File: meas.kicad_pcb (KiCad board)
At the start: 2 copper layers, 100 x 135 mm, 218 parts, among them J101 Conn_01x06_Socket, J102 Conn_01x02_Socket, J103 Conn_01x02_Socket, J104 Conn_01x02_Socket, J105 Conn_01x02_Socket, Q1001 DPLS350E, U1001 MC7805, U1101 R05C05TE05S, U1201 R05C05TE05S, U1301 R05C05TE05S, U1401 R05C05TE05S, U201 Si8641BD-B-IS2, U301 Si8641BD-B-IS2, U401 Si8641BD-B-IS2, U501 Si8641BD-B-IS2, U601 ADS8665IPWR, U701 ADS8665IPWR, U801 ADS8665IPWR, U901 ACS730xLCTR-20AB

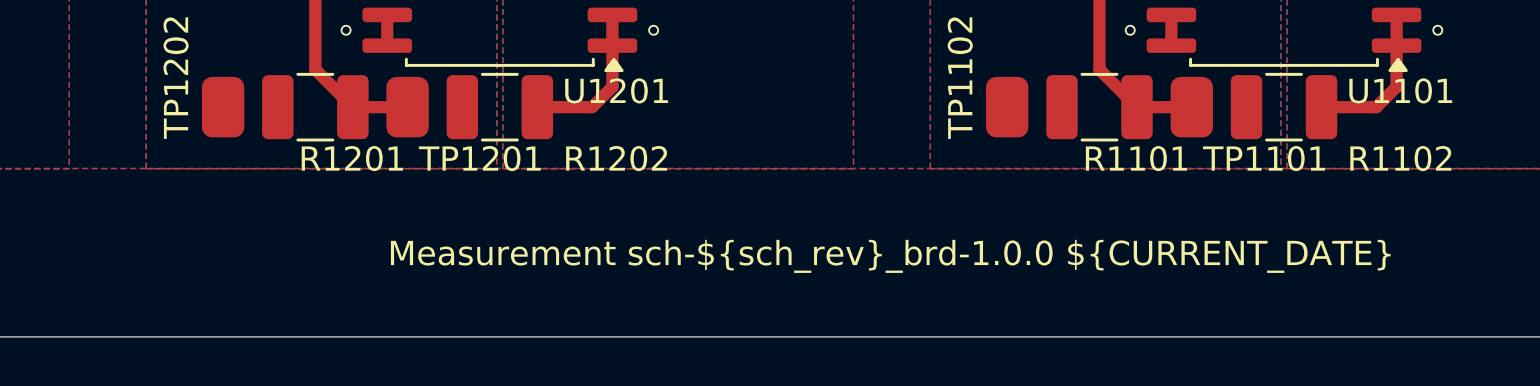
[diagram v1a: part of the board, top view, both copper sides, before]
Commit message: fix netlist error in schematic and layout
GND planes of isodcdc and adc of current measurement were not connected and now are connected.
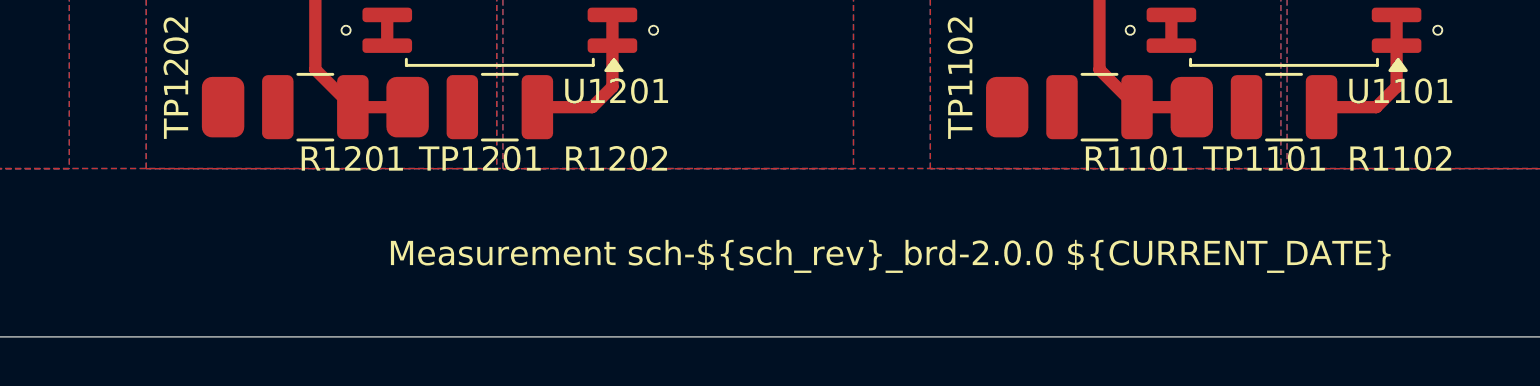
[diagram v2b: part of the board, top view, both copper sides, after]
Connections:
- C1201 pad 1: /adc1/GND_ADC -> /GND_ISO_I
- C1202 pad 1: /adc1/GND_ADC -> /GND_ISO_I
- C701 pad 1: /adc1/GND_ADC -> /GND_ISO_I
- C702 pad 1: /adc1/GND_ADC -> /GND_ISO_I
- C703 pad 1: /adc1/GND_ADC -> /GND_ISO_I
- C705 pad 1: /adc1/GND_ADC -> /GND_ISO_I
- C706 pad 1: /adc1/GND_ADC -> /GND_ISO_I
- C707 pad 1: /adc1/GND_ADC -> /GND_ISO_I
- D1201 pad 2: /adc1/GND_ADC -> /GND_ISO_I
- D701 pad 1: /adc1/GND_ADC -> /GND_ISO_I
- R1201 pad 1: /adc1/GND_ADC -> /GND_ISO_I
- R1202 pad 1: /adc1/GND_ADC -> /GND_ISO_I
- R704 pad 2: /adc1/GND_ADC -> /GND_ISO_I
- TP1202 pad 1: /adc1/GND_ADC -> /GND_ISO_I
- U1201 pad 11: /adc1/GND_ADC -> /GND_ISO_I
- U1201 pad 12: /adc1/GND_ADC -> /GND_ISO_I
- U1201 pad 15: /adc1/GND_ADC -> /GND_ISO_I
- U1201 pad 16: /adc1/GND_ADC -> /GND_ISO_I
- U1201 pad 9: /adc1/GND_ADC -> /GND_ISO_I
- U701 pad 1: /adc1/GND_ADC -> /GND_ISO_I
- U701 pad 3: /adc1/GND_ADC -> /GND_ISO_I
- U701 pad 5: /adc1/GND_ADC -> /GND_ISO_I
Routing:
- net /GND_ISO_I: track 165.9 -> 265.7 mm, vias 8 -> 14
- net /adc1/GND_ADC: track 99.8 -> 0.00 mm, vias 6 -> 0
- removed copper zone on B.Cu, net /adc1/GND_ADC
- removed copper zone on F.Cu, net /adc1/GND_ADC
